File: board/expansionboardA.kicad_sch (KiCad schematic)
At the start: 66 parts, among them J1 USB_C_Receptacle, J2 USB_A_Stacked, J3 HDMI_A, J4 USB_C_Receptacle, SW1 ESPPROG, U1 MAX3420EECJ, U2 GPIO_U2, U3 SII164CTG64, U4 GPIO_U4, U5 ESP32-C6-WROOM-1-N8, U6 CS4344-CZZR, U7 MAX3421EEHJ+T, Y1 403C35D12M00000, Y2 403C35D12M00000

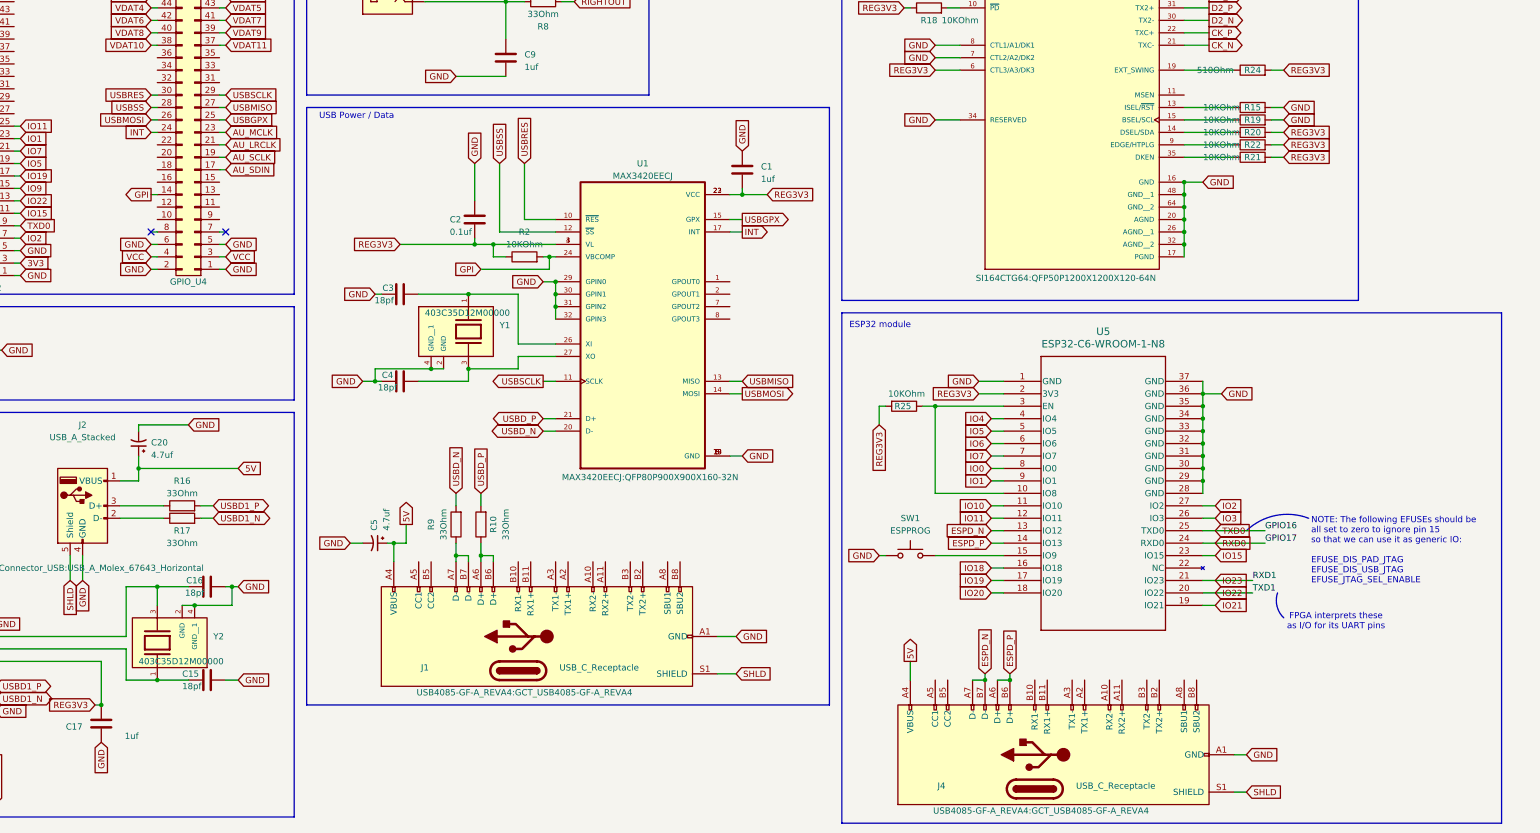
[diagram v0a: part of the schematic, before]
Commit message: Updated gateware, ROM version, and board schematic to remove MAX3420 support
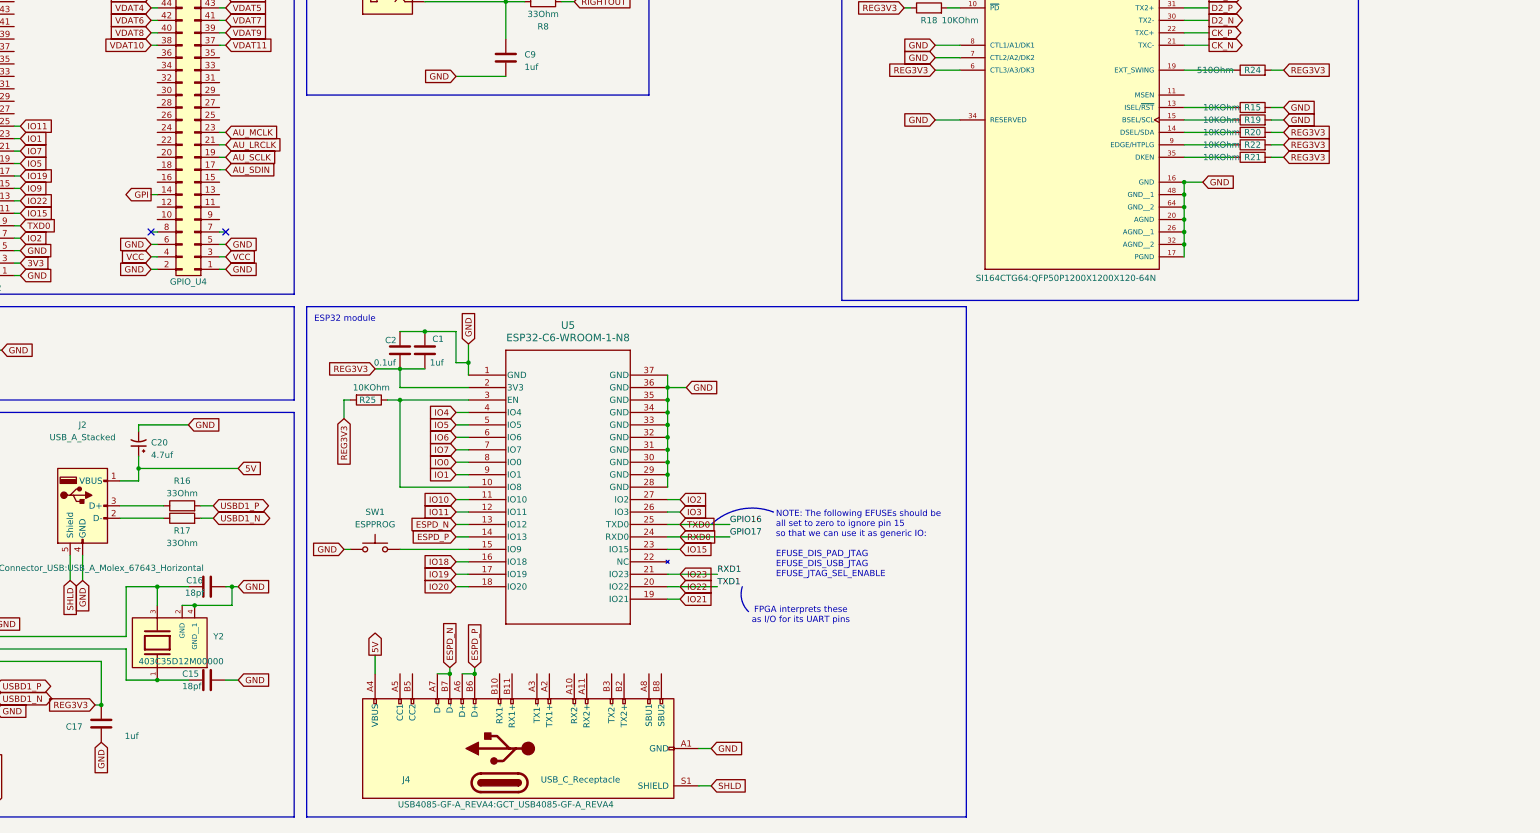
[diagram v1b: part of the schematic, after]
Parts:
- removed C3, C4: 18pf, Capacitor_SMD:C_0603_1608Metric_Pad1.08x0.95mm_HandSolder, symbol Device:C
- removed C5: 4.7uf, Capacitor_SMD:CP_Elec_4x5.4, symbol Device:C_Polarized_Small_US
- removed J1: USB_C_Receptacle, USB4085-GF-A_REVA4:GCT_USB4085-GF-A_REVA4, symbol Connector:USB_C_Receptacle
- removed R10, R9: 33Ohm, Resistor_SMD:R_0603_1608Metric_Pad0.98x0.95mm_HandSolder, symbol Device:R
- removed R2: 10KOhm, Resistor_SMD:R_0603_1608Metric_Pad0.98x0.95mm_HandSolder, symbol Device:R
- removed U1: MAX3420EECJ, MAX3420EECJ:QFP80P900X900X160-32N, symbol MAX3420EECJ:MAX3420EECJ
- removed Y1: 403C35D12M00000, 403C35D12M00000:XTAL_403C35D12M00000, symbol 403C35D12M00000:403C35D12M00000
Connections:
- net INT: no longer names the net of U4.24 (Pin_24)
- net USBGPX: no longer names the net of U4.25 (Pin_25)
- net USBMISO: no longer names the net of U4.27 (Pin_27)
- net USBMOSI: no longer names the net of U4.26 (Pin_26)
- net USBRES: no longer names the net of U4.30 (Pin_30)
- net USBSCLK: no longer names the net of U4.29 (Pin_29)
- net USBSS: no longer names the net of U4.28 (Pin_28)
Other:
- note removed: "USB Power / Data"
- moved on the sheet: J4, R25, SW1, U5

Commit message: More changes to sample
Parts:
- added U1: XC7A35T-FTG256, Package_BGA:Xilinx_FTG256, symbol FPGA_Xilinx_Artix7:XC7A35T-FTG256
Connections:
- net GND: now also U1.A1 (GND), U1.A11 (GND), U1.B8 (GND), U1.C15 (GND), U1.C5 (GND), U1.D12 (GND), U1.D2 (GND), U1.E9 (GND), U1.F10 (GND), U1.F16 (GND), U1.F6 (GND), U1.G13 (GND), U1.G3 (GND), U1.G7 (GNDADC_0), U1.G9 (GND), U1.H6 (GND), U1.J11 (GND), U1.J9 (GND), U1.K14 (GND), U1.K4 (GND), U1.K6 (GND), U1.L1 (GND), U1.L11 (GND), U1.M8 (GND), U1.N15 (GND), U1.N5 (GND), U1.P12 (GND), U1.P2 (GND), U1.R9 (GND), U1.T16 (GND), U1.T6 (GND)
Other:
- moved on the sheet: R15, R18, R19, R20, R21, R22, R23, R24, U3

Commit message: undo board change
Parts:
- removed U1: XC7A35T-FTG256, Package_BGA:Xilinx_FTG256, symbol FPGA_Xilinx_Artix7:XC7A35T-FTG256

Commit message: board update
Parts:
- added C3: 0.1uf, Capacitor_SMD:C_0603_1608Metric_Pad1.08x0.95mm_HandSolder, symbol Device:C
- added SW2: ESPRESET, Button_Switch_SMD:SW_Tactile_SPST_NO_Straight_CK_PTS636Sx25SMTRLFS, symbol Switch:SW_Push
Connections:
- net GND: now also C3.2, SW2.1
- net at R25.1, U5.10 (IO8), U5.3 (EN): now also C3.1, SW2.2

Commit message: Serial port output fix Removed ring buffer Added some SDK functions Fixed a minor hardware inefficiency Updated ROM
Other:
- note added: "ESP32 to SDCard routing: IO1: CS IO4: MOSI IO5: SCK IO6: MISO"
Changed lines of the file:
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@@
+		)
+	)
+	(text "ESP32 to SDCard routing:\nIO1: CS\nIO4: MOSI\nIO5: SCK\nIO6: MISO"
+		(exclude_from_sim no)
+		(at 259.842 183.896 0)
+		(effects
+			(font
+				(size 1.27 1.27)
+			)
+			(justify left)
 		)
 	)

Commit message: moved uart intercept setting to app side (for OS apps)
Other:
- note added: "This pin is supposed to stop ROM logging when low"
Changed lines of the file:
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@@
+	)
+	(arc
+		(start 269.24 213.36)
+		(mid 257.4063 211.1675)
+		(end 246.8 205.48)
+		(stroke
+			(width 0)
+			(type default)
+		)
+		(fill
+			(type none)
+		)
 	)
 	(arc
@@
 		)
 	)
+	(text "This pin is supposed to\nstop ROM logging when low"
+		(exclude_from_sim no)
+		(at 280.924 214.63 0)
+		(effects
+			(font
+				(size 1.27 1.27)
+			)
+		)
+	)

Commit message: ROM updates and a few other cleanups
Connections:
- net MONITORSENSE: now reaches U3.11 (MSEN)
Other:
- note added: "001: 5 step deskew"
- note added: "12bit mode"
- note added: "Dual-edge latch for input data"
- note added: "Enable deskew"
- note added: "I2C disabled"
- note added: "Latch on rising edge"
- note added: "REBOOT to tinysys CPU"
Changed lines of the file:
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@@
 	(wire
 		(pts
+			(xy 92.71 356.87) (xy 113.03 356.87)
+		)
+		(stroke
+			(width 0)
+			(type default)
+		)
+	)
+	(wire
+		(pts
 			(xy 36.83 59.69) (xy 41.91 59.69)
 		)
@@
 		)
 	)
+	(arc
+		(start 177.8 210.82)
+		(mid 182.5244 208.1275)
+		(end 187.96 208.28)
+		(stroke
+			(width 0)
+			(type default)
+		)
+		(fill
+			(type none)
+		)
+	)
 	(rectangle
 		(start 22.86 109.22)
@@
 		)
 	)
+	(text "12bit mode"
+		(exclude_from_sim no)
+		(at 125.222 362.204 0)
+		(effects
+			(font
+				(size 1.27 1.27)
+			)
+		)
+	)
 	(text "Video Output"
 		(exclude_from_sim no)
@@
 		)
 	)
+	(text "REBOOT\nto tinysys CPU"
+		(exclude_from_sim no)
+		(at 176.276 212.852 0)
+		(effects
+			(font
+				(size 1.27 1.27)
+			)
+		)
+	)
+	(text "001:\n5 step deskew"
+		(exclude_from_sim no)
+		(at 27.178 348.234 0)
+		(effects
+			(font
+				(size 1.27 1.27)
+			)
+		)
+	)
 	(text "Micro SD Card"
 		(exclude_from_sim no)
@@
 		)
 	)
+	(text "Latch on rising edge"
+		(exclude_from_sim no)
+		(at 133.35 367.538 0)
+		(effects
+			(font
+				(size 1.27 1.27)
+			)
+		)
+	)
 	(text "USB Host"
 		(exclude_from_sim no)
@@
 		)
 	)
+	(text "I2C disabled"
+		(exclude_from_sim no)
+		(at 125.984 359.664 0)
+		(effects
+			(font
+				(size 1.27 1.27)
+			)
+		)
+	)
 	(text "Status LEDs"
 		(exclude_from_sim no)
@@
 		)
 	)
+	(text "Enable deskew"
+		(exclude_from_sim no)
+		(at 130.302 370.078 0)
+		(effects
+			(font
+				(size 1.27 1.27)
+			)
+		)
+	)
 	(text "This pin is supposed to\nstop ROM logging when low"
 		(exclude_from_sim no)
@@
 		)
 	)
+	(text "Dual-edge latch for input data"
+		(exclude_from_sim no)
+		(at 138.43 364.744 0)
+		(effects
+			(font
+				(size 1.27 1.27)
+			)
+		)
+	)
 	(text "3v3 Power Regulator"
 		(exclude_from_sim no)
@@
 			(effects
 				(font
+					(size 1.27 1.27)
+				)
+				(justify left)
+				(hide yes)
+			)
+		)
+	)
+	(global_label "MONITORSENSE"
+		(shape output)
+		(at 113.03 356.87 0)
+		(fields_autoplaced yes)
+		(effects
+			(font
+				(size 1.27 1.27)
+			)
+			(justify left)
+		)
+		(property "Intersheetrefs" "${INTERSHEET_REFS}"
+			(at 130.348 356.87 0)
+			(effects
+				(font

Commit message: Board updates for version 2G Factory test ROM update
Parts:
- added U1: ESP32-S3, ESP32_S3:QFN56_7X7_EXP-L, symbol ESP32S3:ESP32-S3
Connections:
- net GND: now also U1.57 (GND)
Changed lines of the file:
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@@
 	(wire
 		(pts
+			(xy 265.43 293.37) (xy 269.24 293.37)
+		)
+		(stroke
+			(width 0)
+			(type default)
+		)
+	)
+	(wire
+		(pts
 			(xy 92.71 323.85) (xy 97.79 323.85)
 		)
@@
 		)
 	)
+	(global_label "GND"
+		(shape input)
+		(at 269.24 293.37 0)
+		(fields_autoplaced yes)
+		(effects
+			(font
+				(size 1.27 1.27)
+			)
+			(justify left)
+		)
+		(property "Intersheetrefs" "${INTERSHEET_REFS}"
+			(at 276.0163 293.37 0)
+			(effects
+				(font
+					(size 1.27 1.27)
+				)
+				(justify left)
+				(hide yes)
+			)
+		)
+	)
 	(global_label "IO3"
 		(shape input)
@@
 					(unit 1)
 				)
+			)
+		)
+	)
+	(symbol
+		(lib_id "ESP32S3:ESP32-S3")
+		(at 199.39 293.37 0)
+		(unit 1)
+		(exclude_from_sim no)
+		(in_bom yes)
+		(on_board yes)
+		(dnp no)
+		(fields_autoplaced yes)
+		(property "Reference" "U1"
+			(at 232.41 283.21 0)
+			(effects
+				(font
+					(size 1.524 1.524)
+				)
+			)
+		)
+		(property "Value" "ESP32-S3"
+			(at 232.41 285.75 0)
+			(effects
+				(font
+					(size 1.524 1.524)
+				)
+			)
+		)
+		(property "Footprint" "ESP32_S3:QFN56_7X7_EXP-L"
+			(at 199.39 293.37 0)
+			(effects
+				(font
+					(size 1.27 1.27)
+					(italic yes)
+				)
+				(hide yes)
+			)
+		)
+		(property "Datasheet" "ESP32-S3"
+			(at 199.39 293.37 0)
+			(effects
+				(font
+					(size 1.27 1.27)
+					(italic yes)
+				)
+				(hide yes)
+			)
+		)
+		(property "Description" ""
+			(at 199.39 293.37 0)
+			(effects
+				(font
+					(size 1.27 1.27)
+				)
+				(hide yes)
+			)
+		)
+		(pin "31"
+		)
+		(pin "18"
+		)
+		(pin "51"
+		)
+		(pin "20"
+		)
+		(pin "39"
+		)
+		(pin "43"
+		)
+		(pin "52"
+		)
+		(pin "16"
+		)
+		(pin "28"
+		)
+		(pin "4"
+		)
+		(pin "13"
+		)
+		(pin "35"
+		)
+		(pin "53"
+		)
+		(pin "6"
+		)
+		(pin "55"
+		)
+		(pin "9"
+		)
+		(pin "10"
+		)
+		(pin "2"
+		)
+		(pin "22"
+		)
+		(pin "19"
+		)
+		(pin "34"
+		)
+		(pin "5"
+		)
+		(pin "23"
+		)
+		(pin "45"
+		)
+		(pin "57"
+		)
+		(pin "11"
+		)
+		(pin "24"
+		)
+		(pin "1"
+		)
+		(pin "15"
+		)
+		(pin "27"
+		)
+		(pin "25"
+		)
+		(pin "37"
+		)
+		(pin "36"
+		)
+		(pin "42"
+		)
+		(pin "47"
+		)
+		(pin "41"
+		)
+		(pin "46"
+		)
+		(pin "44"
+		)
+		(pin "29"
+		)
+		(pin "30"
+		)
+		(pin "50"
+		)
+		(pin "17"
+		)
+		(pin "49"
+		)
+		(pin "54"
+		)
+		(pin "56"
+		)
+		(pin "12"
+		)
+		(pin "26"
+		)
+		(pin "32"
+		)
+		(pin "33"
+		)
+		(pin "3"
+		)
+		(pin "38"
+		)
+		(pin "48"
+		)
+		(pin "40"
+		)
+		(pin "7"
+		)
+		(pin "8"
+		)
+		(pin "14"
+		)
+		(pin "21"
+		)
+		(instances
+			(project ""
+				(path "/317f7f3e-4535-46d0-9a87-af1bea12706a"
+					(reference "U1")
+					(unit 1)
+				)
